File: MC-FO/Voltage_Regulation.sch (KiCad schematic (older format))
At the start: 8 parts, among them U19 R-78E5.0-0.5, U20 R-78E3.3-0.5

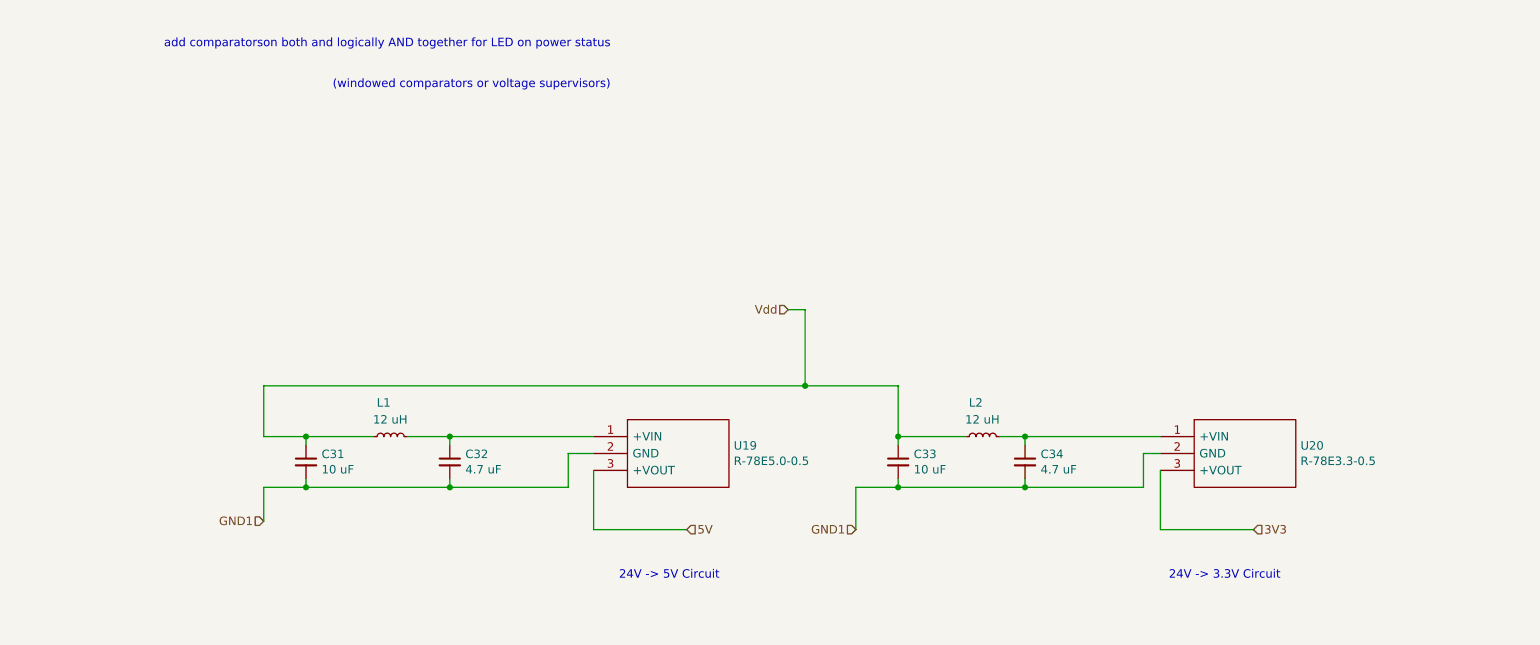
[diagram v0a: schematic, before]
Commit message: unpopulated cap after voltage regulators
and changed reference designator numbering scheme
and moved the or gate that sends 3.3 V to comparator in detector ckt
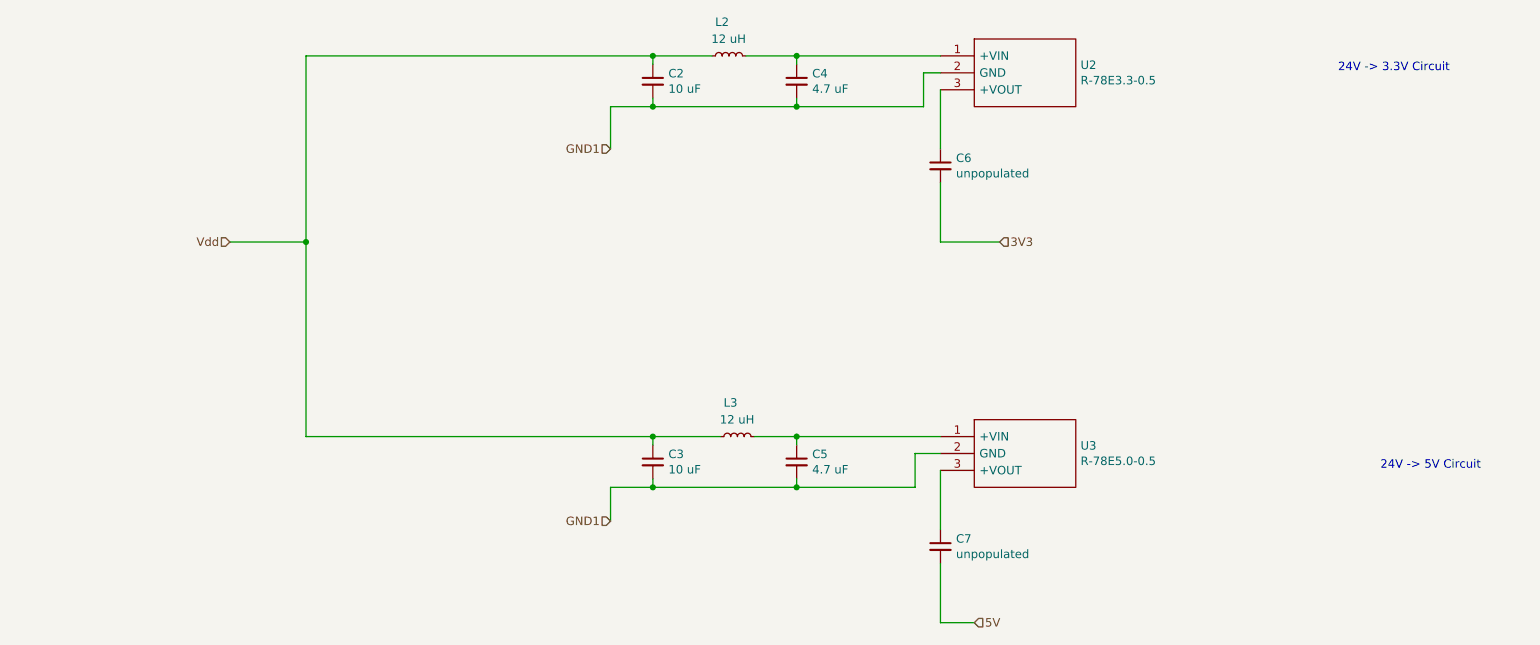
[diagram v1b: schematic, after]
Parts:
- added C6, C7: unpopulated, Capacitor_SMD:C_0603_1608Metric, symbol Device:C_Small
- renumbered C33 to C2, C31 to C3, C34 to C4, C32 to C5, L1 to L3, U20 to U2, U19 to U3
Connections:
- net 3V3: now also C6.2; no longer U2.3 (+VOUT)
- net 5V: now also C7.2; no longer U3.3 (+VOUT)
- new net: C6.1, U2.3 (+VOUT)
- new net: C7.1, U3.3 (+VOUT)
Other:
- note removed: "add comparatorson both and logically AND together for LED on power status\n\n\n (windowed comparators or voltage supervisors)"
- moved on the sheet: C2, C3, C4, C5, L2, L3, U2, U3

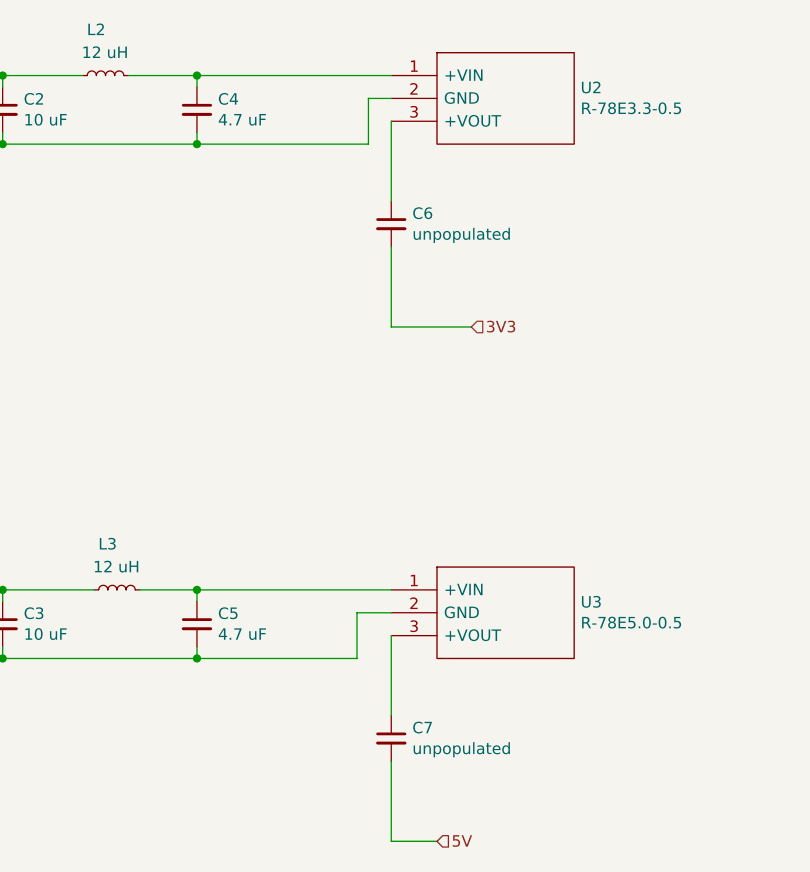
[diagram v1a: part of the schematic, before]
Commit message: Fixed file hierarchy
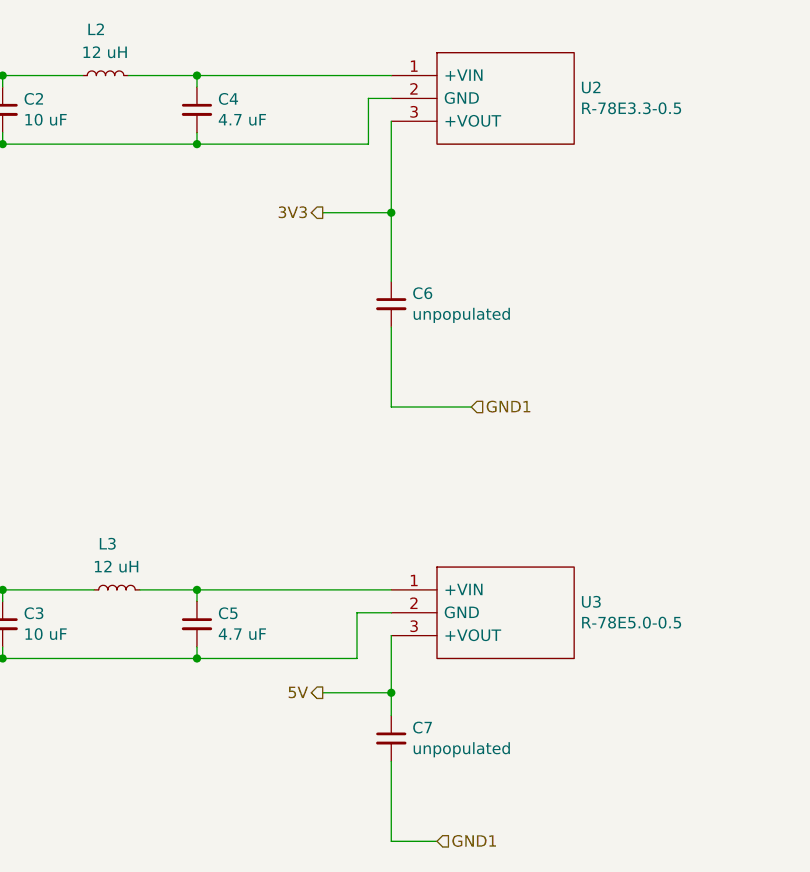
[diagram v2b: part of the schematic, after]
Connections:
- net 3V3: now also C6.1, U2.3 (+VOUT); no longer C6.2
- net 5V: now also C7.1, U3.3 (+VOUT); no longer C7.2
- net GND1: now also C6.2, C7.2
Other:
- moved on the sheet: C6
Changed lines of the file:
@@
 $Descr A4 11693 8268
 encoding utf-8
-Sheet 10 11
+Sheet 11 11
 Title ""
 Date ""
@@
 	3700 4900 3700 5100
 Wire Wire Line
-	5650 4800 5650 5150
-Wire Wire Line
-	5650 2550 5650 2900
-Text HLabel 6000 3450 2    50   Input ~ 0
+	5650 4800 5650 5050
+Text HLabel 5350 2950 0    50   Output ~ 0
 3V3
-Text HLabel 5850 5700 2    50   Input ~ 0
+Text HLabel 5350 5050 0    50   Output ~ 0
 5V
 Text HLabel 3700 5100 0    50   Input ~ 0
@@
 L Device:C_Small C6
 U 1 1 617C87F8
-P 5650 3000
-F 0 "C6" H 5742 3046 50  0000 L CNN
-F 1 "unpopulated" H 5742 2955 50  0000 L CNN
-F 2 "Capacitor_SMD:C_0603_1608Metric" H 5650 3000 50  0001 C CNN
-F 3 "~" H 5650 3000 50  0001 C CNN
-	1    5650 3000
-	1    0    0    -1
-$EndComp
-Wire Wire Line
-	5650 3100 5650 3450
-Wire Wire Line
-	5650 3450 6000 3450
+P 5650 3350
+F 0 "C6" H 5742 3396 50  0000 L CNN
+F 1 "unpopulated" H 5742 3305 50  0000 L CNN
+F 2 "Capacitor_SMD:C_0603_1608Metric" H 5650 3350 50  0001 C CNN
+F 3 "~" H 5650 3350 50  0001 C CNN
+	1    5650 3350
+	1    0    0    -1
+$EndComp
+Wire Wire Line
+	5650 3450 5650 3800
+Wire Wire Line
+	5650 3800 6000 3800
 Text HLabel 1450 3450 0    50   Input ~ 0
 Vdd
@@
 Wire Wire Line
 	3700 2650 3950 2650
+Text HLabel 6000 3800 2    50   Input ~ 0
+GND1
+Text HLabel 5850 5700 2    50   Input ~ 0
+GND1
+Wire Wire Line
+	5650 3250 5650 2950
+Wire Wire Line
+	5650 2550 5650 2950
+Wire Wire Line
+	5650 2950 5350 2950
+Connection ~ 5650 2950
+Wire Wire Line
+	5650 5050 5350 5050
+Connection ~ 5650 5050
+Wire Wire Line
+	5650 5050 5650 5150
 $EndSCHEMATC

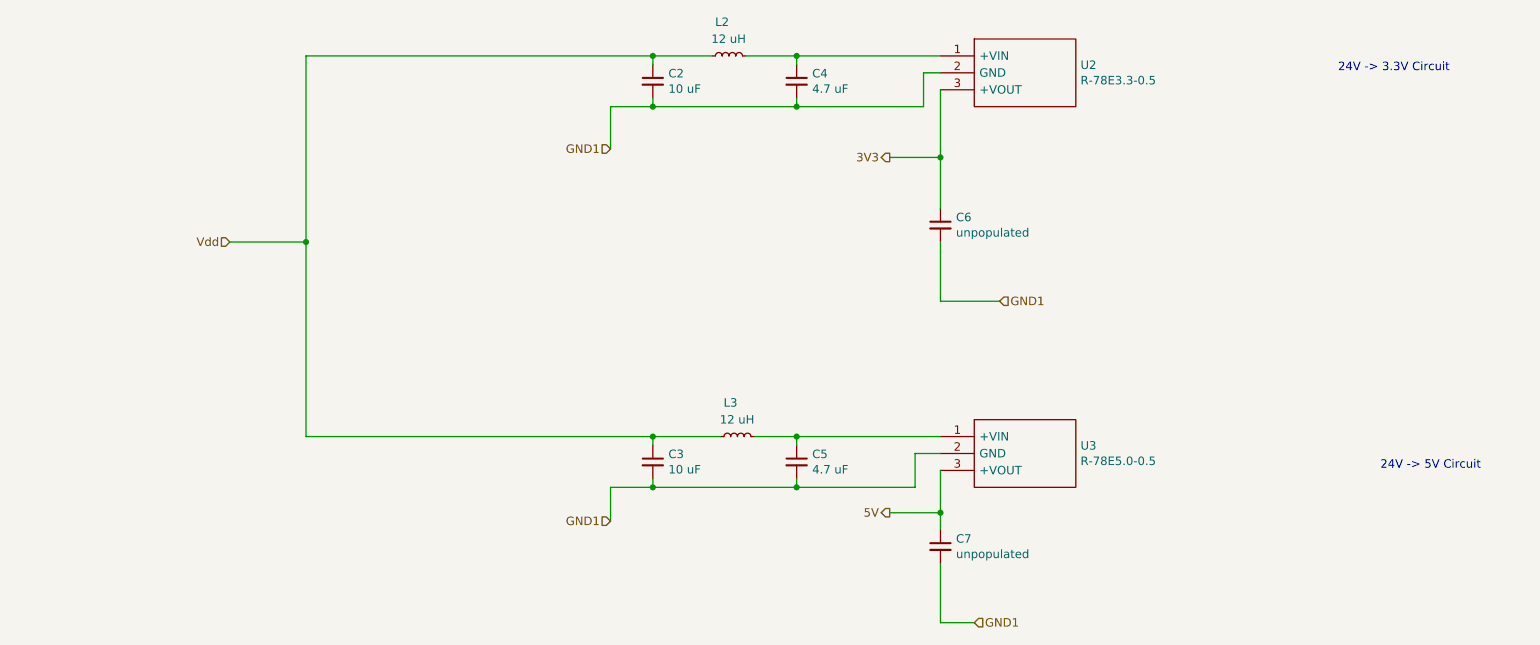
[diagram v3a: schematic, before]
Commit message: changed status1 to output of detector
reassigned footprint of 550 LED
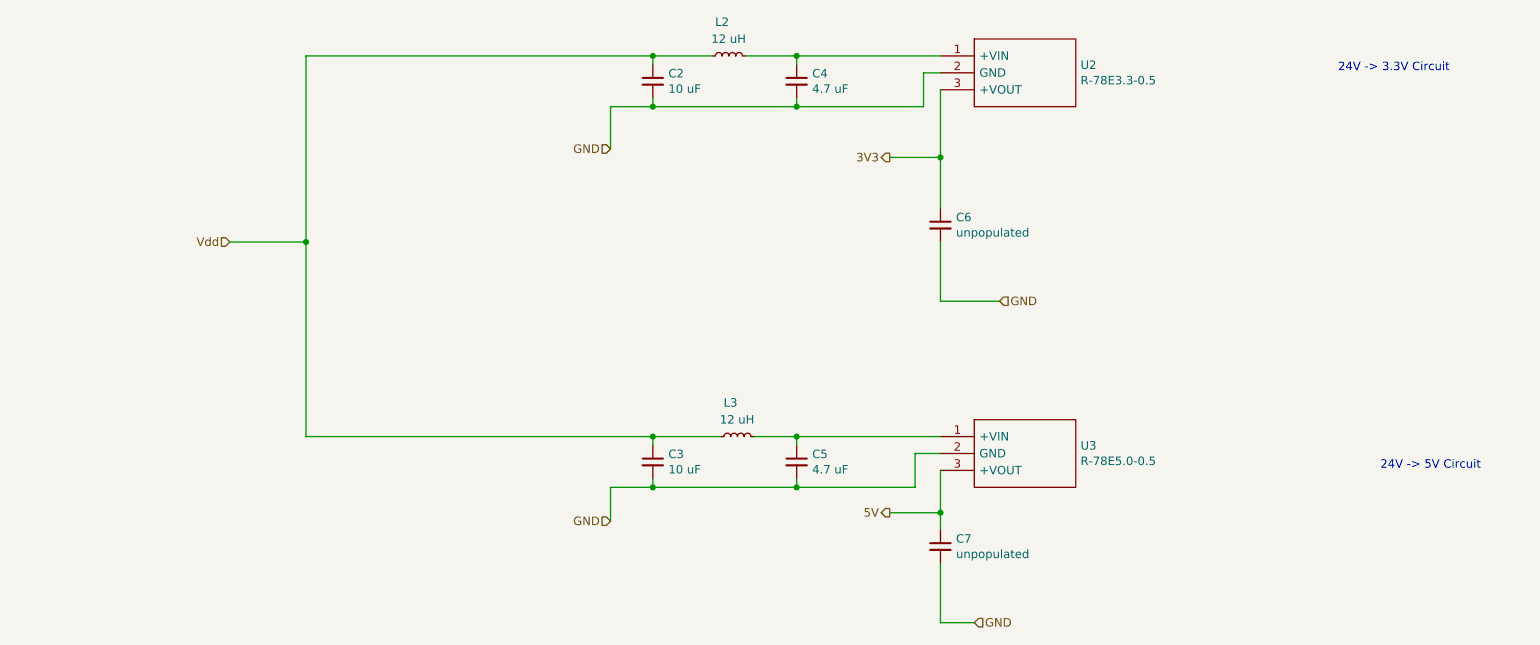
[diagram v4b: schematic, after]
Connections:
- net GND1 renamed GND
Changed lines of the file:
@@
 5V
 Text HLabel 3700 5100 0    50   Input ~ 0
-GND1
+GND
 Text HLabel 3700 2900 0    50   Input ~ 0
-GND1
+GND
 $Comp
 L Device:L_Small L3
@@
 	3700 2650 3950 2650
 Text HLabel 6000 3800 2    50   Input ~ 0
-GND1
+GND
 Text HLabel 5850 5700 2    50   Input ~ 0
-GND1
+GND
 Wire Wire Line
 	5650 3250 5650 2950

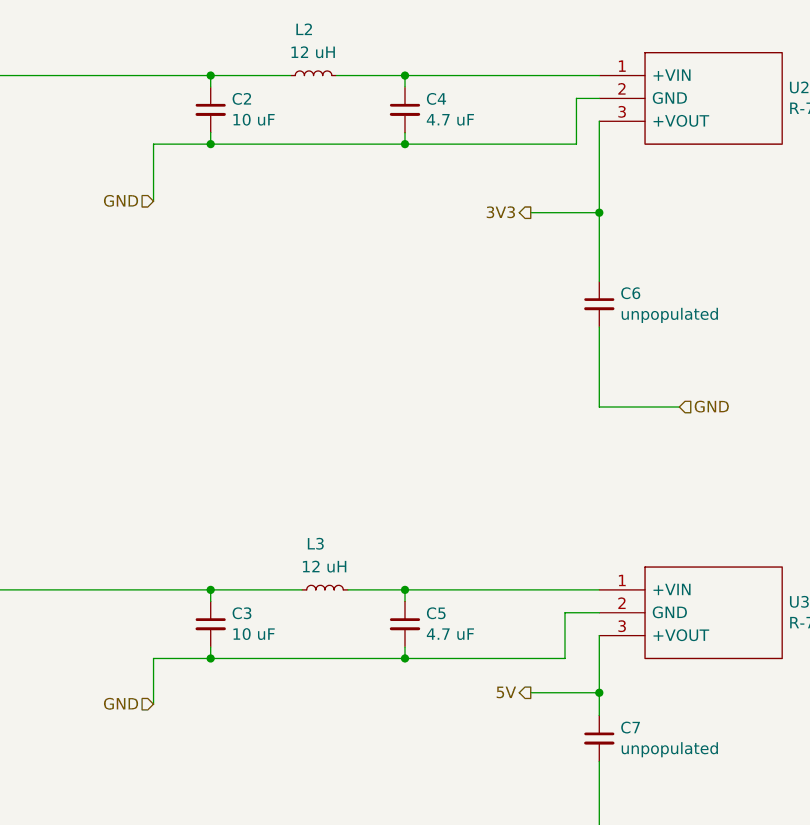
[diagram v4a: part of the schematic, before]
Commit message: DSP schem, FO schem, and FO layout changes
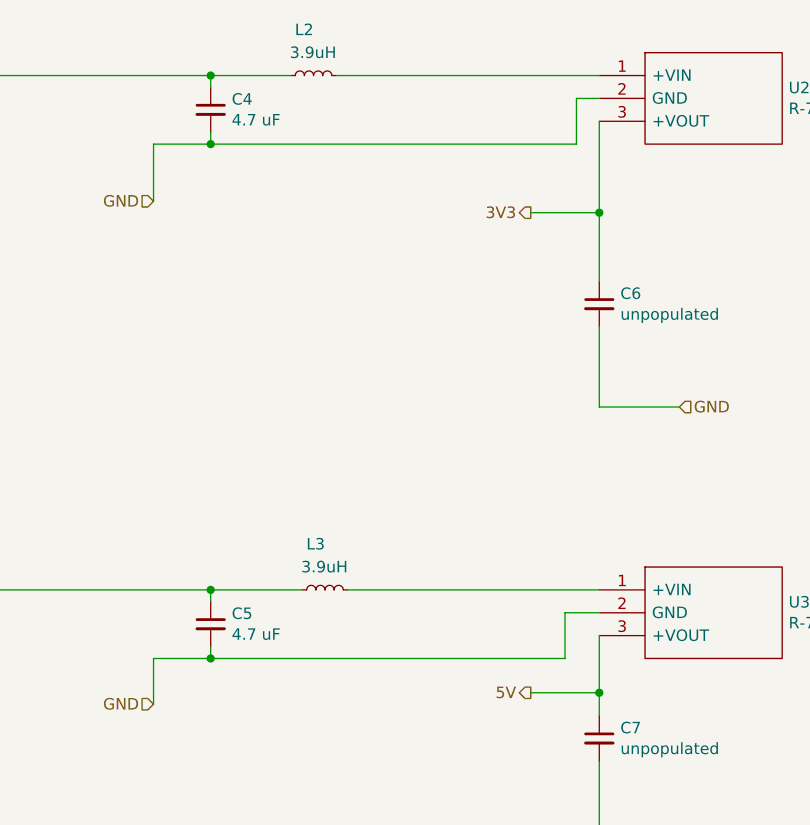
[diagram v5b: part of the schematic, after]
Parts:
- removed C2, C3: 10 uF, Capacitor_SMD:C_1210_3225Metric, symbol Device:C_Small
- C6, C7: footprint Capacitor_SMD:C_0603_1608Metric -> Capacitor_SMD:C_1210_3225Metric
- L2, L3: value 12 uH -> 3.9uH; footprint Inductor_SMD:L_0603_1608Metric -> Inductor_SMD:L_1812_4532Metric_Pad1.30x3.40mm_HandSolder
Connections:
- net Vdd: now also C4.1, C5.1
- net at L3.2, U3.1 (+VIN): no longer C5.1
- net at L2.2, U2.1 (+VIN): no longer C4.1
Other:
- moved on the sheet: C4, C5
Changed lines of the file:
@@
 Text HLabel 3700 2900 0    50   Input ~ 0
 GND
-$Comp
-L Device:L_Small L3
-U 1 1 61767909
-P 4450 4600
-F 0 "L3" V 4650 4600 50  0000 L CNN
-F 1 "12 uH" V 4550 4500 50  0000 L CNN
-F 2 "Inductor_SMD:L_0603_1608Metric" H 4450 4600 50  0001 C CNN
-F 3 "~" H 4450 4600 50  0001 C CNN
-	1    4450 4600
-	0    -1   -1   0
-$EndComp
-Wire Wire Line
-	4550 4600 4800 4600
-Wire Wire Line
-	4800 4600 4800 4650
-Wire Wire Line
-	4800 4600 5650 4600
-Connection ~ 4800 4600
-Wire Wire Line
-	4800 4900 4800 4850
-Wire Wire Line
-	4800 4900 5500 4900
 Wire Wire Line
 	5500 4900 5500 4700
 Wire Wire Line
 	5500 4700 5650 4700
-Connection ~ 4800 4900
 $Comp
 L Device:L_Small L2
@@
 P 4400 2350
 F 0 "L2" V 4600 2350 50  0000 L CNN
-F 1 "12 uH" V 4500 2250 50  0000 L CNN
-F 2 "Inductor_SMD:L_0603_1608Metric" H 4400 2350 50  0001 C CNN
-F 3 "~" H 4400 2350 50  0001 C CNN
+F 1 "3.9uH" V 4500 2250 50  0000 L CNN
+F 2 "Inductor_SMD:L_1812_4532Metric_Pad1.30x3.40mm_HandSolder" H 4400 2350 50  0001 C CNN
+F 3 "https://www.digikey.com/en/products/detail/recom-power/RLS-126/9920565" H 4400 2350 50  0001 C CNN
 	1    4400 2350
 	0    -1   -1   0
@@
 	3950 2350 3950 2400
 Wire Wire Line
-	4500 2350 4800 2350
-Wire Wire Line
-	4800 2350 4800 2400
-Wire Wire Line
 	3950 2650 3950 2600
-Wire Wire Line
-	3950 2650 4800 2650
-Wire Wire Line
-	4800 2650 4800 2600
 Connection ~ 3950 2650
-Wire Wire Line
-	4800 2350 5650 2350
-Connection ~ 4800 2350
-Wire Wire Line
-	4800 2650 5550 2650
 Wire Wire Line
 	5550 2650 5550 2450
 Wire Wire Line
 	5550 2450 5650 2450
-Connection ~ 4800 2650
 $Comp
 L Existing_IC_Models:R-78E5.0-0.5 U3
@@
 Connection ~ 3950 4900
 Wire Wire Line
-	3950 4900 4800 4900
-Wire Wire Line
 	3700 4900 3950 4900
-Wire Wire Line
-	3950 4900 3950 4850
-$Comp
-L Device:C_Small C3
-U 1 1 617DD2CC
-P 3950 4750
-F 0 "C3" H 4042 4796 50  0000 L CNN
-F 1 "10 uF" H 4042 4705 50  0000 L CNN
-F 2 "Capacitor_SMD:C_1210_3225Metric" H 3950 4750 50  0001 C CNN
-F 3 "~" H 3950 4750 50  0001 C CNN
-	1    3950 4750
-	1    0    0    -1
-$EndComp
 Wire Wire Line
 	4350 4600 3950 4600
@@
 Connection ~ 3950 4600
 $Comp
-L Device:C_Small C5
-U 1 1 617DF962
-P 4800 4750
-F 0 "C5" H 4892 4796 50  0000 L CNN
-F 1 "4.7 uF" H 4892 4705 50  0000 L CNN
-F 2 "Capacitor_SMD:C_1210_3225Metric" H 4800 4750 50  0001 C CNN
-F 3 "~" H 4800 4750 50  0001 C CNN
-	1    4800 4750
-	1    0    0    -1
-$EndComp
-$Comp
 L Device:C_Small C4
 U 1 1 617E1CA5
-P 4800 2500
-F 0 "C4" H 4892 2546 50  0000 L CNN
-F 1 "4.7 uF" H 4892 2455 50  0000 L CNN
-F 2 "Capacitor_SMD:C_1210_3225Metric" H 4800 2500 50  0001 C CNN
-F 3 "~" H 4800 2500 50  0001 C CNN
-	1    4800 2500
-	1    0    0    -1
-$EndComp
-$Comp
-L Device:C_Small C2
-U 1 1 617E2200
 P 3950 2500
-F 0 "C2" H 4042 2546 50  0000 L CNN
-F 1 "10 uF" H 4042 2455 50  0000 L CNN
+F 0 "C4" H 4042 2546 50  0000 L CNN
+F 1 "4.7 uF" H 4042 2455 50  0000 L CNN
 F 2 "Capacitor_SMD:C_1210_3225Metric" H 3950 2500 50  0001 C CNN
 F 3 "~" H 3950 2500 50  0001 C CNN
@@
 F 0 "C7" H 5742 5296 50  0000 L CNN
 F 1 "unpopulated" H 5742 5205 50  0000 L CNN
-F 2 "Capacitor_SMD:C_0603_1608Metric" H 5650 5250 50  0001 C CNN
+F 2 "Capacitor_SMD:C_1210_3225Metric" H 5650 5250 50  0001 C CNN
 F 3 "~" H 5650 5250 50  0001 C CNN
 	1    5650 5250
@@
 F 0 "C6" H 5742 3396 50  0000 L CNN
 F 1 "unpopulated" H 5742 3305 50  0000 L CNN
-F 2 "Capacitor_SMD:C_0603_1608Metric" H 5650 3350 50  0001 C CNN
+F 2 "Capacitor_SMD:C_1210_3225Metric" H 5650 3350 50  0001 C CNN
 F 3 "~" H 5650 3350 50  0001 C CNN
 	1    5650 3350
@@
 Wire Wire Line
 	5650 5050 5650 5150
+$Comp
+L Device:L_Small L3
+U 1 1 61A83391
+P 4450 4600
+F 0 "L3" V 4650 4600 50  0000 L CNN
+F 1 "3.9uH" V 4550 4500 50  0000 L CNN
+F 2 "Inductor_SMD:L_1812_4532Metric_Pad1.30x3.40mm_HandSolder" H 4450 4600 50  0001 C CNN
+F 3 "https://www.digikey.com/en/products/detail/recom-power/RLS-126/9920565" H 4450 4600 50  0001 C CNN
+	1    4450 4600
+	0    -1   -1   0
+$EndComp
+Wire Wire Line
+	3950 4900 3950 4850
+$Comp
+L Device:C_Small C5
+U 1 1 617DF962
+P 3950 4750
+F 0 "C5" H 4042 4796 50  0000 L CNN
+F 1 "4.7 uF" H 4042 4705 50  0000 L CNN
+F 2 "Capacitor_SMD:C_1210_3225Metric" H 3950 4750 50  0001 C CNN
+F 3 "~" H 3950 4750 50  0001 C CNN
+	1    3950 4750
+	1    0    0    -1
+$EndComp
+Wire Wire Line
+	4500 2350 5650 2350
+Wire Wire Line
+	3950 2650 5550 2650
+Wire Wire Line
+	4550 4600 5650 4600
+Wire Wire Line
+	3950 4900 5500 4900
 $EndSCHEMATC

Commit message: Add files via upload
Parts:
- added TP21: TestPoint, TestPoint:TestPoint_Pad_D2.0mm, symbol Connector:TestPoint
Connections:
- net Vdd: now also TP21.1
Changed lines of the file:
@@
 $Descr A4 11693 8268
 encoding utf-8
-Sheet 10 10
+Sheet 9 11
 Title ""
 Date ""
@@
 Connection ~ 3950 2350
 Wire Wire Line
-	1450 3450 1900 3450
+	1450 3450 1600 3450
 Connection ~ 1900 3450
 Wire Wire Line
@@
 Wire Wire Line
 	3950 4900 5500 4900
+$Comp
+L Connector:TestPoint TP21
+U 1 1 623D8FE0
+P 1600 3450
+F 0 "TP21" H 1658 3568 50  0000 L CNN
+F 1 "TestPoint" H 1658 3477 50  0000 L CNN
+F 2 "TestPoint:TestPoint_Pad_D2.0mm" H 1800 3450 50  0001 C CNN
+F 3 "~" H 1800 3450 50  0001 C CNN
+	1    1600 3450
+	1    0    0    -1
+$EndComp
+Connection ~ 1600 3450
+Wire Wire Line
+	1600 3450 1900 3450
 $EndSCHEMATC
